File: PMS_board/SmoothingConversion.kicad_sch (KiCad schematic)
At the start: 27 parts, among them U22 AP63203WU7, U23 DCP3603ACMR, U24 AP63205QWU7

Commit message: Divided Bulk Caps
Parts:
- removed C23, C24, C25: 1000uF, symbol Device:C_Polarized_US
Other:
- note added: "Fuse"
- note removed: "Bulk Capacitors"

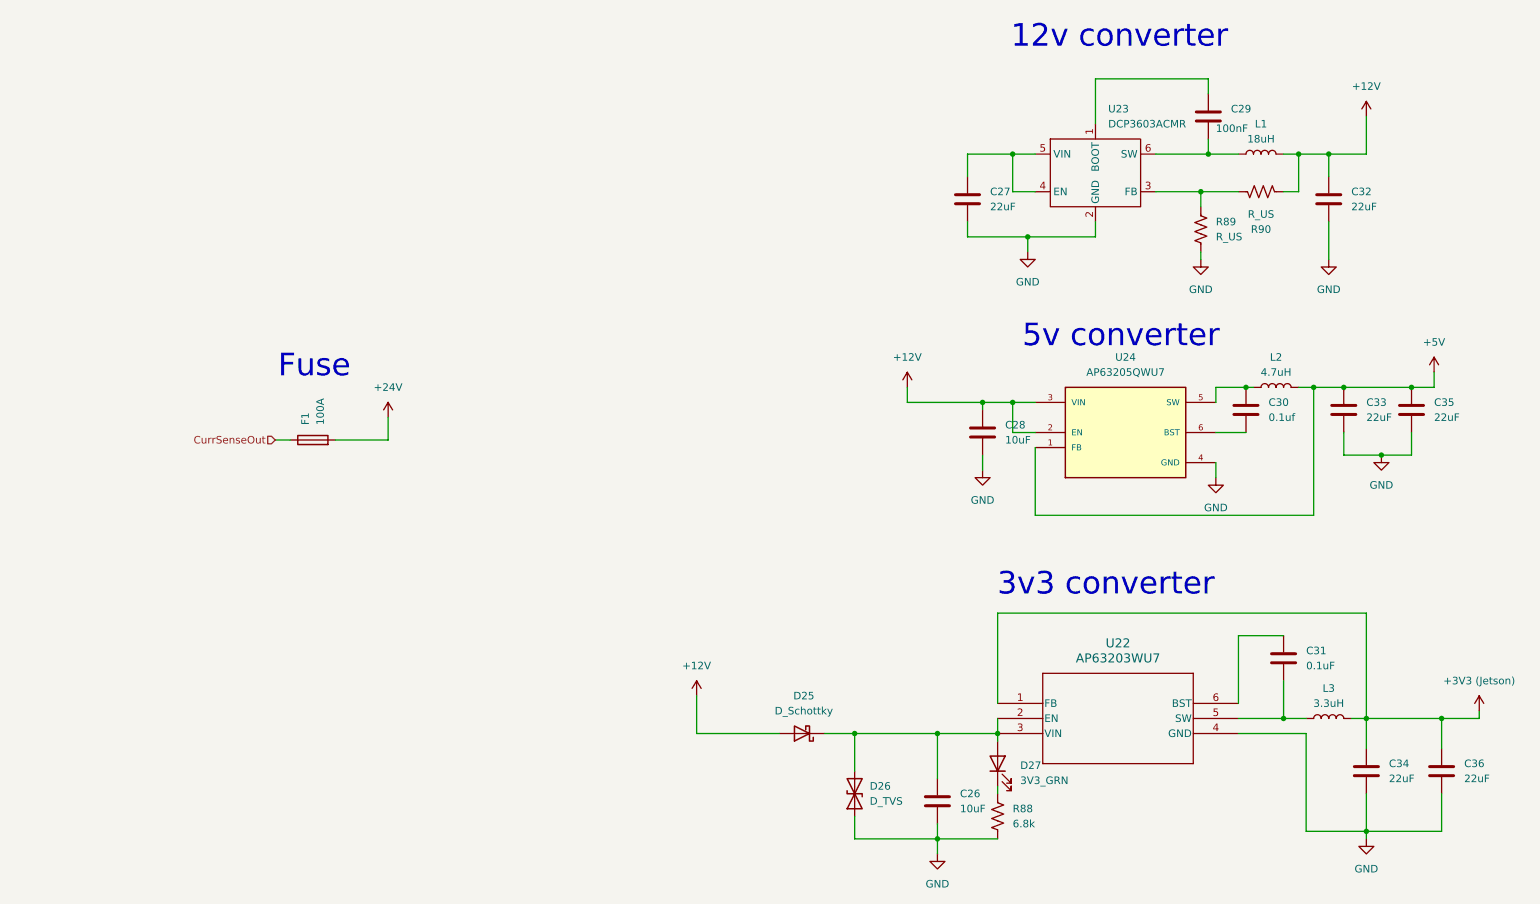
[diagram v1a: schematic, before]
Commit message: Add Fuse, made things look nice
I added fuse symbol, footprint, and datasheet. I organized 2 sheets and condensed schematics
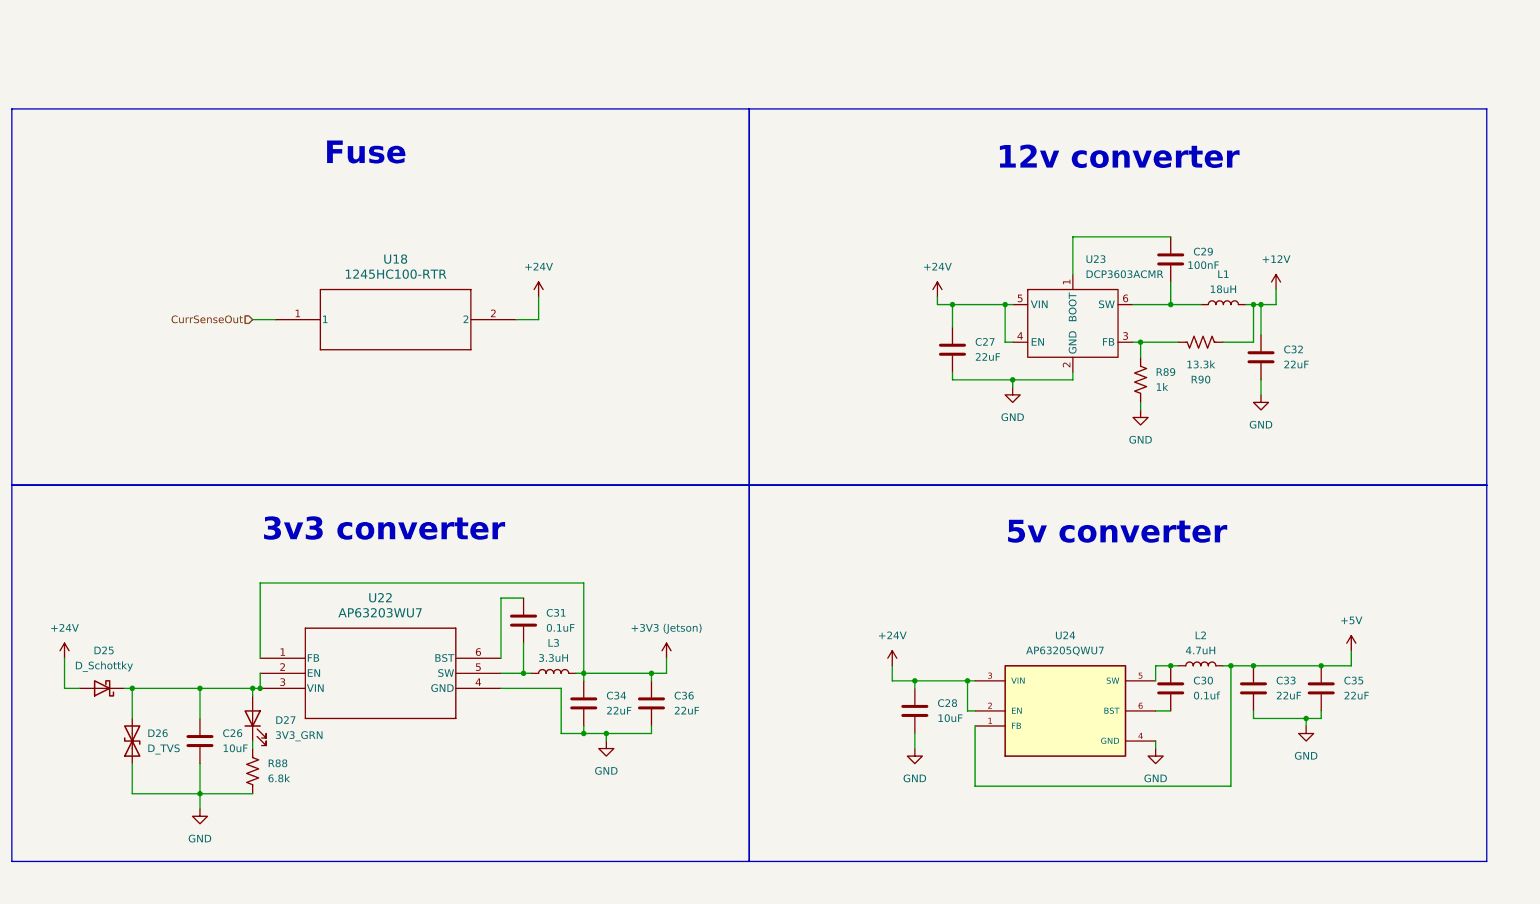
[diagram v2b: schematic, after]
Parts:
- removed F1: 100A, symbol Device:Fuse
- added U18: 1245HC100-RTR, 1245HC100-RTR_COB, symbol 1245HC100-RTR_COB:1245HC100-RTR
- R89: value R_US -> 1k
- R90: value R_US -> 13.3k
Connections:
- net +12V: no longer C28.1, D25.2 (A), U24.2 (EN), U24.3 (VIN)
- net +24V: now also C27.1, C28.1, D25.2 (A), U23.4 (EN), U23.5 (VIN), U24.2 (EN), U24.3 (VIN), U18.2
- net CurrSenseOut: now also U18.1
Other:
- moved on the sheet: C26, C27, C28, C29, C30, C31, C32, C33, C34, C35, C36, D25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

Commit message: Spec'ed TVSs and added more footprints
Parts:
- U18: footprint 1245HC100-RTR_COB -> 1245HC100-RTR_COB:1245HC100-RTR_COB
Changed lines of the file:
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@@
 			)
 		)
-		(property "Footprint" "1245HC100-RTR_COB"
+		(property "Footprint" "1245HC100-RTR_COB:1245HC100-RTR_COB"
 			(at 67.31 68.58 0)
 			(hide yes)

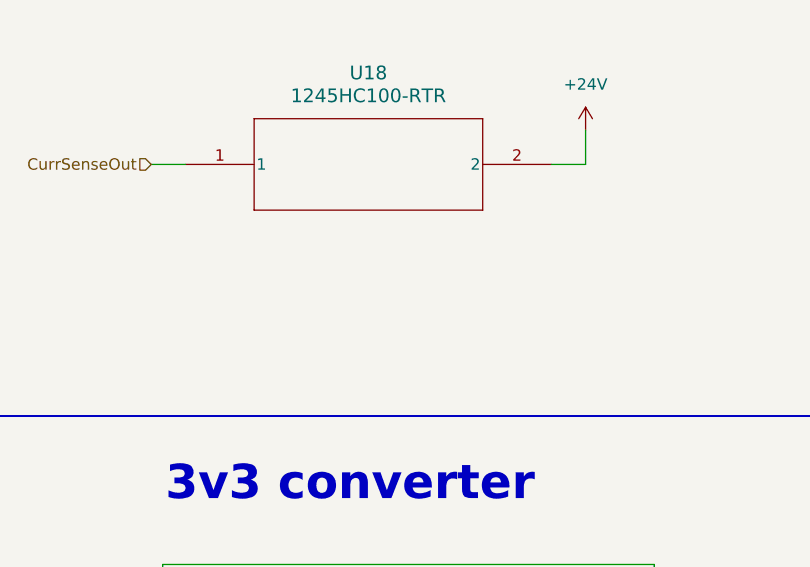
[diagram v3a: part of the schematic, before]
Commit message: Fuse BAD
change fuse
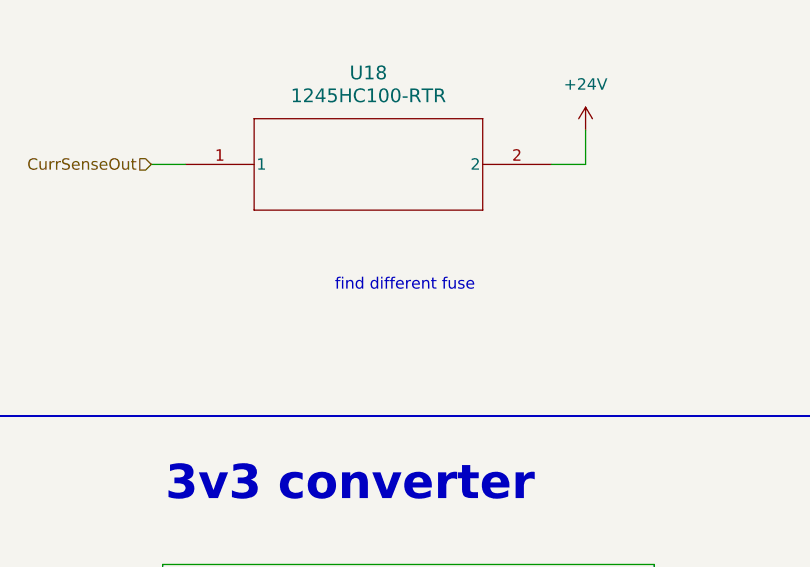
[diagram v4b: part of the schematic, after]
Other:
- note added: "find different fuse"
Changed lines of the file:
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@@
+		)
+	)
+	(text "find different fuse\n"
+		(exclude_from_sim no)
+		(at 91.694 82.042 0)
+		(effects
+			(font
+				(size 1.27 1.27)
+			)
 		)
 	)

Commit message: Footprints for connectors and new resistors
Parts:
- L2: footprint (none) -> Inductor_SMD:L_Bourns_SRR1210A
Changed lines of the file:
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@@
 			)
 		)
-		(property "Footprint" ""
+		(property "Footprint" "Inductor_SMD:L_Bourns_SRR1210A"
 			(at 223.52 127 0)
 			(hide yes)

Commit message: Change based on Will's input
respeced buck
swapped to molex_sls
readded 6-pole switch
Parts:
- removed D27: 3V3_GRN, Diode_SMD:D_0603_1608Metric_Pad1.05x0.95mm_HandSolder, symbol Device:LED
- removed L3: 3.3uH, Inductor_SMD:L_1812_4532Metric_Pad1.30x3.40mm_HandSolder, symbol Device:L
- removed R88: 6.8k, Resistor_SMD:R_0603_1608Metric_Pad0.98x0.95mm_HandSolder, symbol Device:R_US
- added L4: 3.9uH, Inductor_SMD:L_1812_4532Metric_Pad1.30x3.40mm_HandSolder, symbol Device:L
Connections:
- net +3V3 (Jetson): now also L4.2
- net at C31.2, U22.5 (SW): now also L4.1
